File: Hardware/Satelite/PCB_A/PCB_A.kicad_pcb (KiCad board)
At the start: 2 copper layers, 54 x 54 mm, 87 parts, among them J1 Batería LiPo (Soldada), J2 CONUFL001-SMD, J3 Servo Globo, J4 Conector_PCB_A-B, J5 Servo Paracaídas, M1 Spacer, M2 Spacer, M3 Spacer, Q1 SSM3J338R,LF, Q2 BC817, U1 A2235-H, U2 CC1101RGP, U3 0915BM15A0001E, U4 AP9211SA-AF-HAC-7, U5 B39921B3588U410, U6 CC1190, Y1 26 MHz

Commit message: Completado nuevo PCB_A
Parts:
- removed the C1 at (-0.51, -3.42)
- removed the C13 at (-38.6, 24.2)
- removed the C13 at (9.30, 15.1)
- removed the C14 at (13.8, 16.1)
- removed the L1 at (-44.9, 12.7)
- removed the L1 at (10.9, 16.7)
- removed the R10 at (12.1, 15.7)
- removed the R9 at (-44.9, 9.83)
- removed the R9 at (10.9, 14.6)
- removed TP3: TestPoint_P1, TestPoint:TestPoint_Pad_D1.0mm
- added C13: 0.8pF, Capacitor_SMD:C_0402_1005Metric, F.Cu at (7.90, 0.94)
- added G***: LOGO, AXTEC:Logo_AXTEC, F.Cu at (10.9, 17.3)
- added G***: LOGO, AXTEC:Logo_AXTEC, B.Cu at (10.7, 17.3)
- added L1: Bead, Inductor_SMD:L_0402_1005Metric, F.Cu at (13.1, -0.33)
- added R9: 3.3k, Resistor_SMD:R_0402_1005Metric, F.Cu at (2.57, -3.12)
- moved REF** 62.0 mm to (4.34, 11.2)
- moved L3 59.1 mm to (10.4, -2.36), turned to 180 degrees
- moved REF** 58.0 mm to (-8.97, 20.7)
- moved U5 54.2 mm to (7.44, 3.94), turned to 180 degrees
- moved C14 53.8 mm to (7.09, -0.99), turned to 0 degrees
- moved C17 52.8 mm to (4.50, -3.10)
- moved C16 52.7 mm to (10.4, -0.94), turned to 0 degrees
- moved U6 51.8 mm to (1.80, 0.94), turned to 0 degrees
- moved D3 50.9 mm to (0.11, -25.5), turned to 0 degrees
- moved L4 50.6 mm to (6.25, -2.67), turned to 180 degrees
- moved C2 48.7 mm to (-15.6, 16.2)
- moved R3 48.7 mm to (-19.5, 14.2)
- moved C3 48.7 mm to (-15.6, 14.3)
- moved R4 48.7 mm to (-11.7, 13.0)
- moved U1 48.7 mm to (-4.55, 12.1)
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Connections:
- L5 pad 1: +3V3_Internal -> /CC1101/VDD_PA
- U6 pad 6: /CC1101/VDD_PA -> +3V3_Internal
- U6 pad 7: /CC1101/GDO2 -> /CC1101/GDO0
- U6 pad 8: /CC1101/GDO0 -> /CC1101/GDO2
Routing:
- net +3V3_Internal: track 20.5 -> 132.6 mm, vias 1 -> 2
- net /nCHG: track 0.00 -> 47.8 mm
- net +BATT: track 22.7 -> 68.3 mm, vias 4 -> 5
- net /CC1101/GDO0: track 0.00 -> 41.3 mm, vias 0 -> 4
- net GND: track 91.2 -> 124.9 mm, vias 25 -> 36
- net /CC1101/GDO2: track 0.00 -> 30.1 mm, vias 0 -> 4
- net Net-(J4-Pad14): track 0.00 -> 29.0 mm
- net /CS: track 28.5 -> 56.9 mm, vias 2 -> 0
- net Net-(J4-Pad13): track 0.00 -> 22.1 mm
- net /CC1101/VDD_PA: track 0.00 -> 19.1 mm
- net Net-(R6-Pad1): track 0.00 -> 17.6 mm
- net /GPS_TX: track 0.14 -> 15.5 mm, vias 0 -> 2
- net Net-(R7-Pad1): track 0.00 -> 14.5 mm
- net /SDI: track 37.0 -> 26.6 mm
- net Net-(R5-Pad1): track 0.00 -> 10.3 mm
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- added copper zone on F.Cu, net Net-(L2-Pad2)
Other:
- board text added: "PCB_A v2.0"
- board text removed: "BATT"
- board text removed: "PCB_A v1.0"

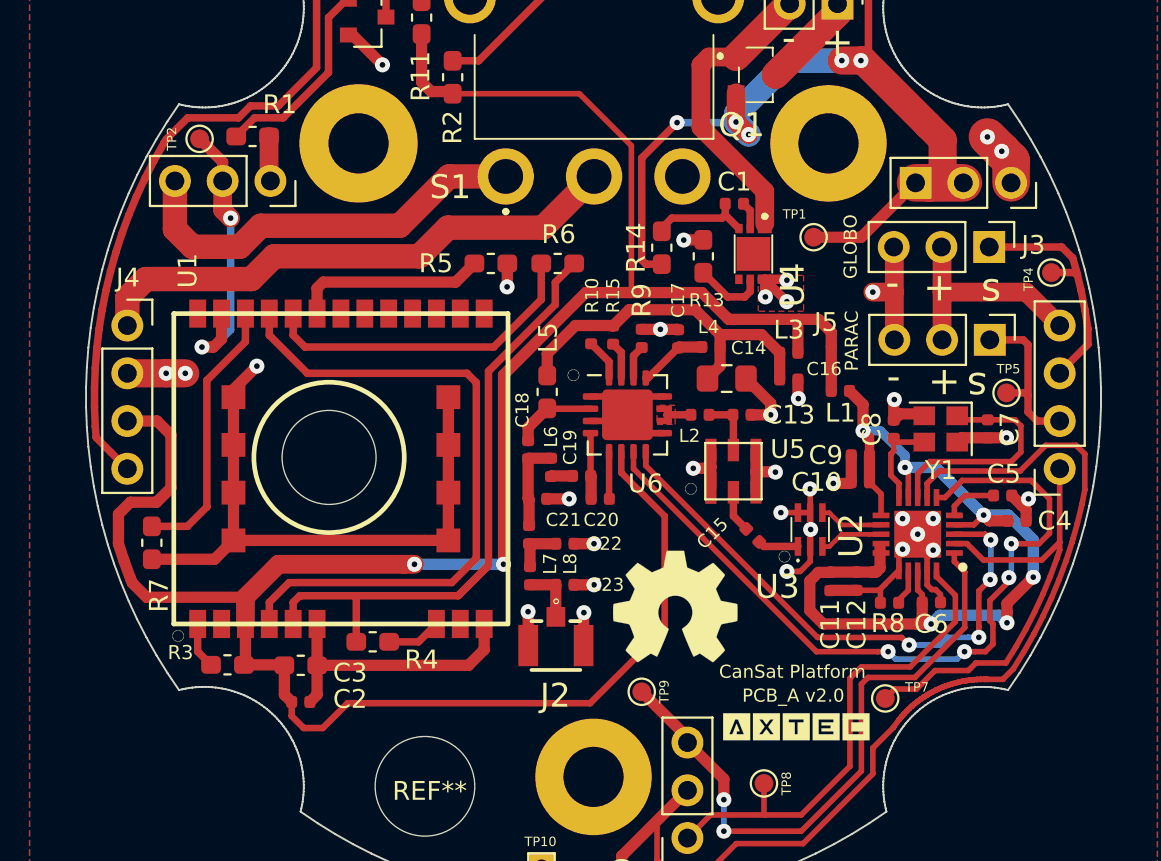
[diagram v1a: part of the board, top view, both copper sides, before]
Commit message: Mejoras al layout RF de PCB_A
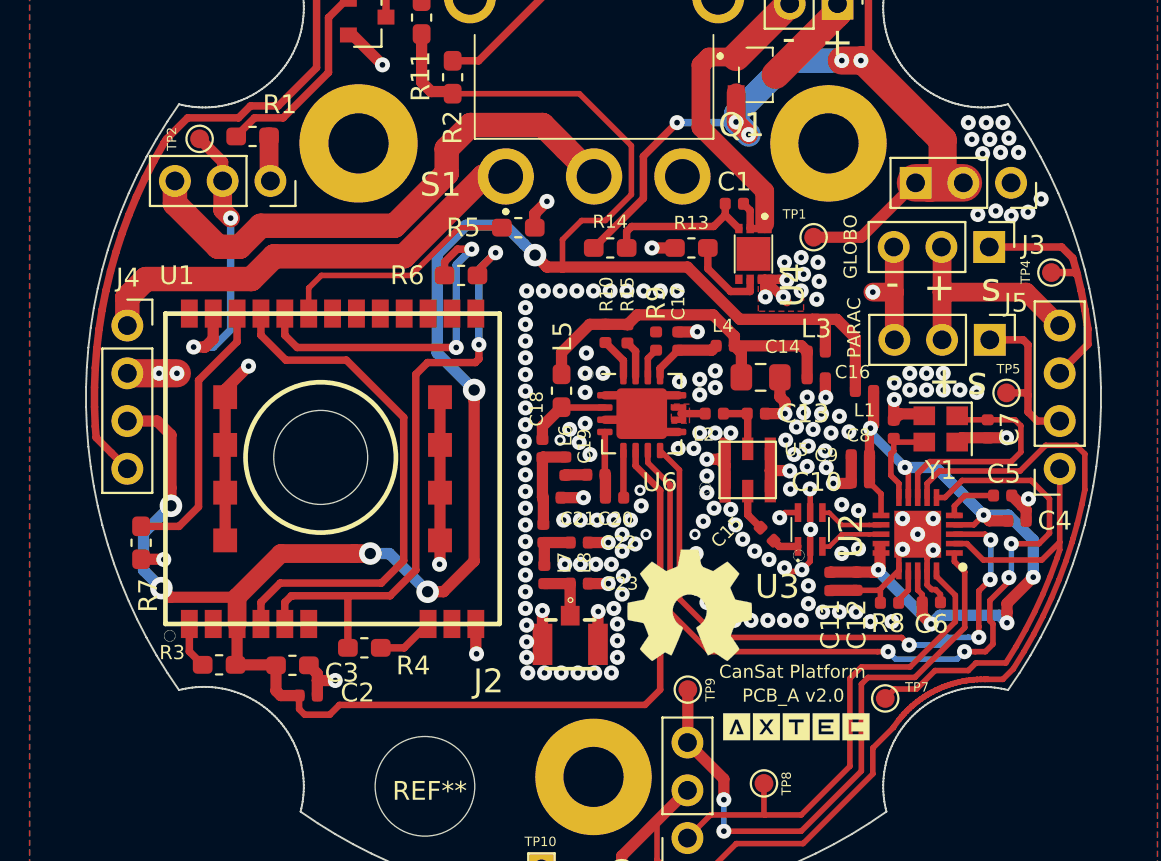
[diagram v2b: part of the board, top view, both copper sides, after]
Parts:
- moved R6 5.18 mm to (-7.05, -6.48)
- moved R14 2.74 mm to (0.89, -7.94), turned to 180 degrees
- moved TP9 2.45 mm to (5.02, 15.6)
- moved R5 2.40 mm to (-4.00, -9.02)
- moved C14 1.80 mm to (8.89, -1.05)
- moved C16 1.46 mm to (11.8, -1.00)
- moved L3 1.46 mm to (11.8, -2.43)
- moved L1 1.28 mm to (14.4, -0.33)
- moved R13 0.78 mm to (5.21, -7.94), turned to 0 degrees
- moved R9 0.77 mm to (3.33, -2.98)
- moved REF** 0.76 mm to (5.11, 11.1)
- moved C13 0.76 mm to (8.66, 0.88)
- moved C15 0.76 mm to (9.23, 7.29)
- moved U5 0.76 mm to (8.20, 3.87)
- moved C23 0.76 mm to (-0.76, 9.92)
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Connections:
- S1 pad 1: Net-(J4-Pad13) -> Net-(J4-Pad14)
- S1 pad 2: Net-(J4-Pad14) -> Net-(J4-Pad13)
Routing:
- net GND: track 124.9 -> 96.2 mm, vias 36 -> 193
- net +3V3_Internal: track 132.6 -> 144.5 mm, vias 2 -> 6
- net Net-(U1-Pad19): track 35.7 -> 27.8 mm
- net Net-(J4-Pad13): track 22.1 -> 29.0 mm
- net VDD: track 49.9 -> 43.5 mm, vias 6 -> 7
- net Net-(J4-Pad14): track 29.0 -> 24.3 mm
- net /CC1101/GDO0: track 41.3 -> 44.4 mm
- net /CC1101/GDO2: track 30.1 -> 32.9 mm
- net Net-(C1-Pad1): track 5.28 -> 8.10 mm
- net Net-(R5-Pad1): track 10.3 -> 13.0 mm
- net /GPS/GPS_1V8: track 34.8 -> 33.0 mm, vias 0 -> 2
- net Net-(R6-Pad1): track 17.6 -> 18.6 mm, vias 0 -> 2
- net Net-(C1-Pad2): track 17.4 -> 18.2 mm
- net +BATT: track 68.3 -> 67.5 mm
- net Net-(C15-Pad2): track 2.16 -> 1.43 mm
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
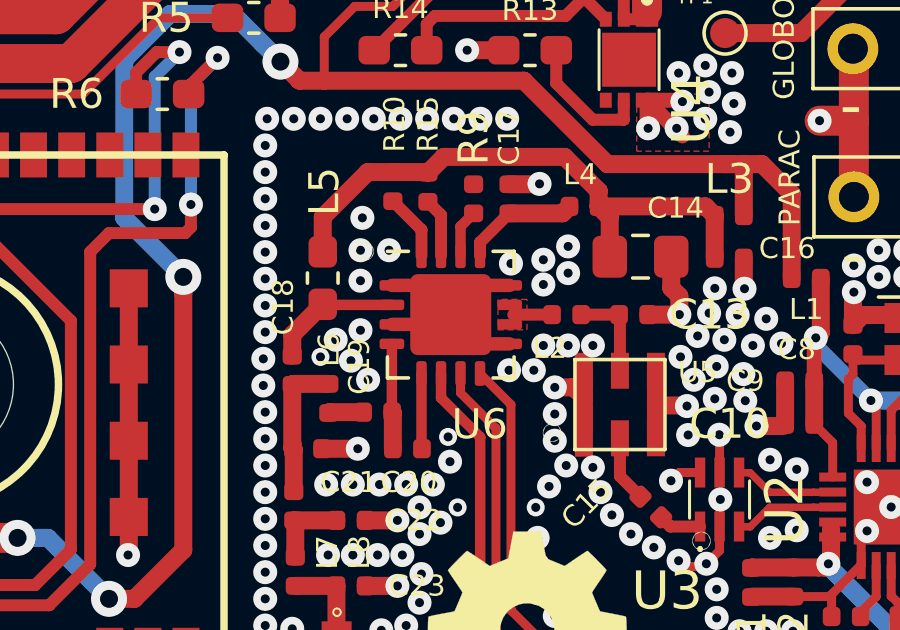
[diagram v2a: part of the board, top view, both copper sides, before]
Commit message: Nuevo PCB de estación terrena con CC1190
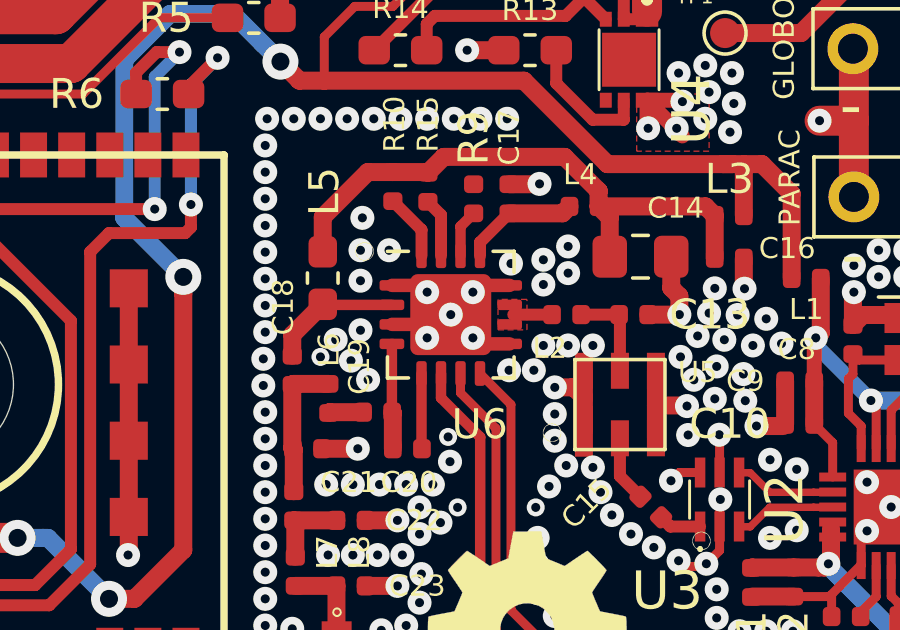
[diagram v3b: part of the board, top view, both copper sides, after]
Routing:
- net GND: vias 193 -> 198
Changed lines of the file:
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@@
     (thickness 1.6)
     (drawings 39)
-    (tracks 942)
+    (tracks 947)
     (zones 0)
     (modules 82)
@@
     (effects (font (size 0.7 0.7) (thickness 0.175)))
   )
+  (via (at 2.5654 0.8763) (size 0.8) (drill 0.3) (layers F.Cu B.Cu) (net 1))
+  (via (at 3.302 0.127) (size 0.8) (drill 0.3) (layers F.Cu B.Cu) (net 1))
+  (via (at 3.302 1.651) (size 0.8) (drill 0.3) (layers F.Cu B.Cu) (net 1))
+  (via (at 1.778 1.651) (size 0.8) (drill 0.3) (layers F.Cu B.Cu) (net 1))
+  (via (at 1.778 0.127) (size 0.8) (drill 0.3) (layers F.Cu B.Cu) (net 1))
   (via (at -1.778 2.286) (size 0.6) (drill 0.3) (layers F.Cu B.Cu) (net 1))
   (via (at 7.3025 1.905) (size 0.8) (drill 0.3) (layers F.Cu B.Cu) (net 1))
@@
     (connect_pads (clearance 0.25))
     (min_thickness 0.25)
-    (fill yes (arc_segments 32) (thermal_gap 0.3) (thermal_bridge_width 0.8))
+    (fill yes (arc_segments 32) (thermal_gap 0.25) (thermal_bridge_width 0.8))
     (polygon
       (pts
@@
     (connect_pads (clearance 0.25))
     (min_thickness 0.25)
-    (fill yes (arc_segments 32) (thermal_gap 0.3) (thermal_bridge_width 0.8))
+    (fill yes (arc_segments 32) (thermal_gap 0.25) (thermal_bridge_width 0.8))
     (polygon
       (pts

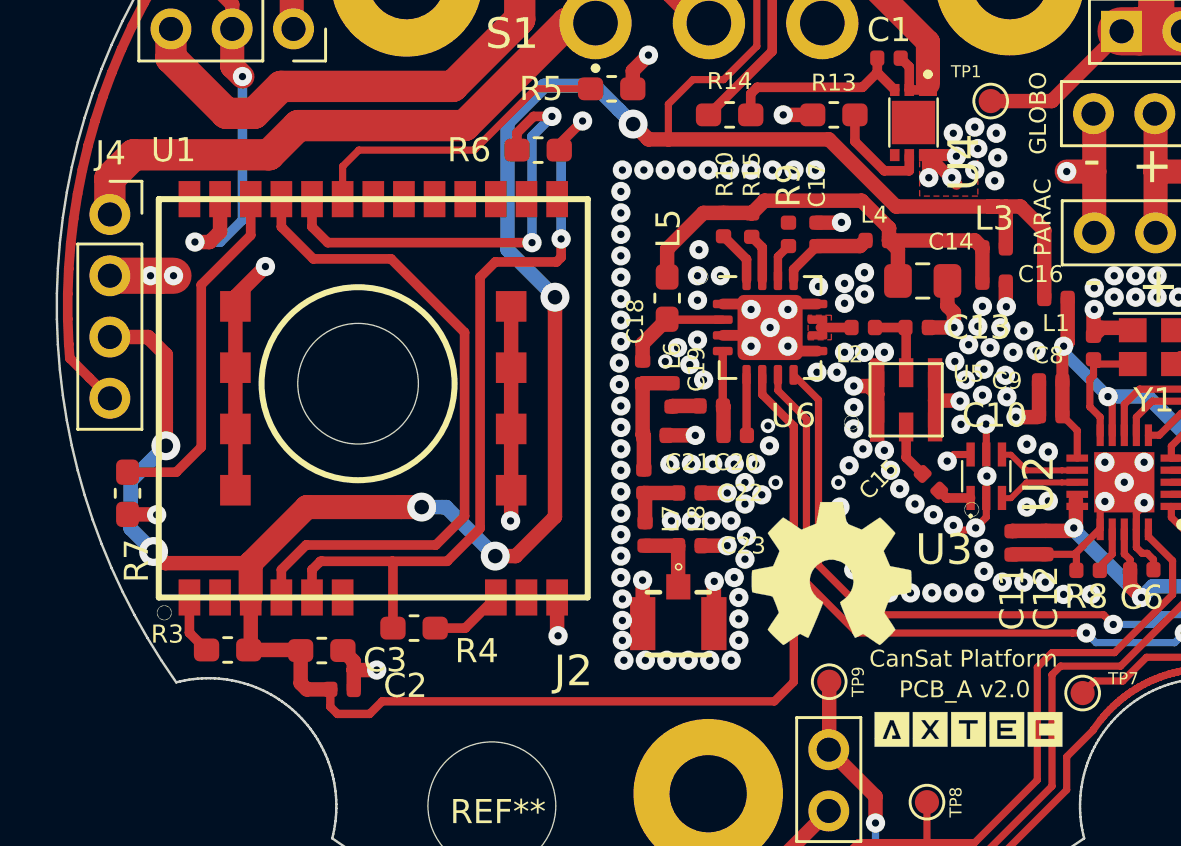
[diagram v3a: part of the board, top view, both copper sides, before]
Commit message: Corrección de silkscreen PCB_C
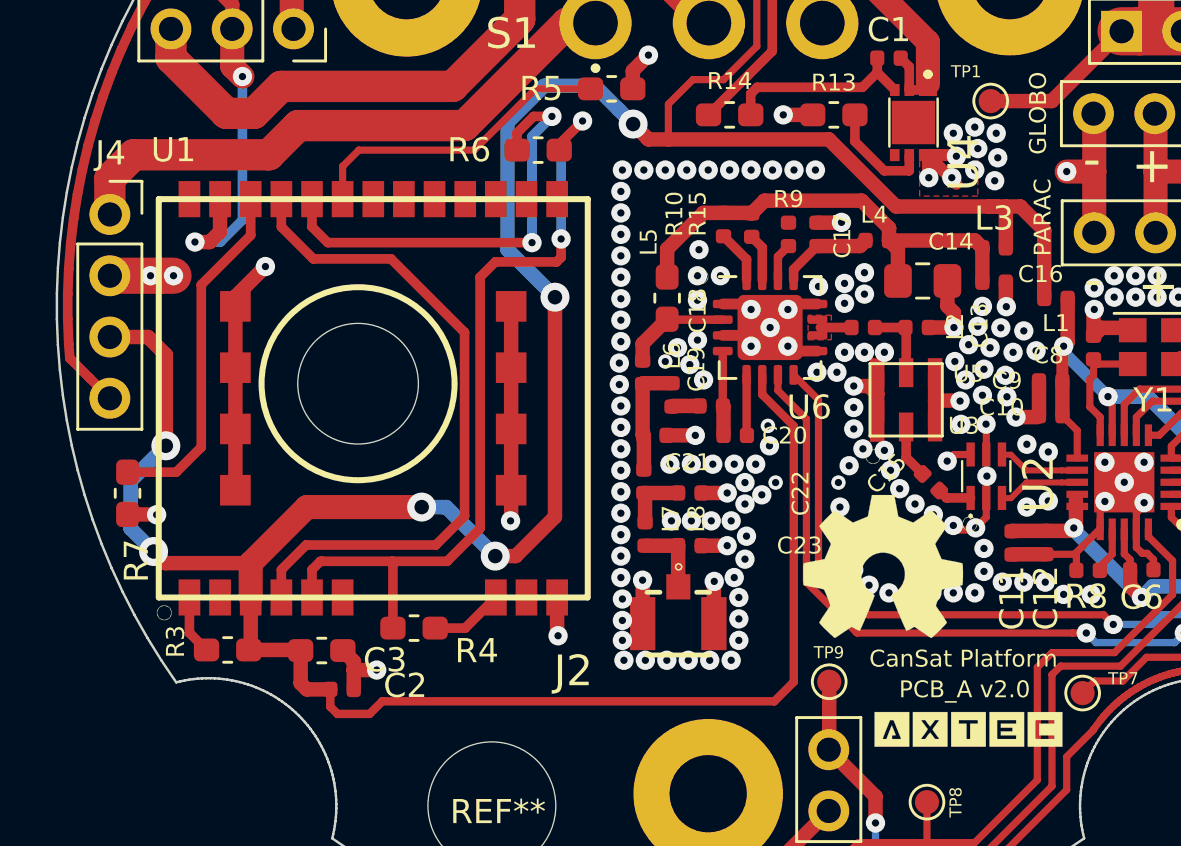
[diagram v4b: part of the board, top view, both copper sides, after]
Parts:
- moved REF** 2.15 mm to (7.24, 10.8)
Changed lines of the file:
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@@
     (tags "QFN NoLead")
     (attr smd)
-    (fp_text reference U6 (at 0.9652 3.6576) (layer F.SilkS)
+    (fp_text reference U6 (at 1.6256 3.3147) (layer F.SilkS)
       (effects (font (size 1 1) (thickness 0.15)))
     )
@@
     (tags resistor)
     (attr smd)
-    (fp_text reference R15 (at 2.1058 0 90) (layer F.SilkS)
+    (fp_text reference R15 (at 0.4675 -2.2352 90) (layer F.SilkS)
       (effects (font (size 0.7 0.7) (thickness 0.15)))
     )
@@
     (tags resistor)
     (attr smd)
-    (fp_text reference R10 (at 2.0828 0.0508 90) (layer F.SilkS)
+    (fp_text reference R10 (at 0.4445 -2.032 90) (layer F.SilkS)
       (effects (font (size 0.7 0.7) (thickness 0.15)))
     )
@@
     (tags resistor)
     (attr smd)
-    (fp_text reference R9 (at 2.032 0 90) (layer F.SilkS)
-      (effects (font (size 1 1) (thickness 0.15)))
+    (fp_text reference R9 (at 1.4605 0 180) (layer F.SilkS)
+      (effects (font (size 0.7 0.7) (thickness 0.15)))
     )
     (fp_text value 3.3k (at 0 1.17 90) (layer F.Fab)
@@
     (tags "inductor handsolder")
     (attr smd)
-    (fp_text reference L5 (at -2.8842 -0.0508 270) (layer F.SilkS)
-      (effects (font (size 1 1) (thickness 0.15)))
+    (fp_text reference L5 (at -2.3241 0.762 270) (layer F.SilkS)
+      (effects (font (size 0.7 0.7) (thickness 0.15)))
     )
     (fp_text value 22nH (at 0 1.43 270) (layer F.Fab)
@@
     (tags inductor)
     (attr smd)
-    (fp_text reference L2 (at 0.5588 -1.1176 180) (layer F.SilkS)
+    (fp_text reference L2 (at -3.81 0.0381 270) (layer F.SilkS)
       (effects (font (size 0.7 0.7) (thickness 0.15)))
     )
@@
     (tags capacitor)
     (attr smd)
-    (fp_text reference C23 (at 2.2074 0) (layer F.SilkS)
+    (fp_text reference C23 (at 4.5442 0) (layer F.SilkS)
       (effects (font (size 0.7 0.7) (thickness 0.15)))
     )
@@
     (tags capacitor)
     (attr smd)
-    (fp_text reference C22 (at 2.1058 0) (layer F.SilkS)
+    (fp_text reference C22 (at 4.595 0.0127 90) (layer F.SilkS)
       (effects (font (size 0.7 0.7) (thickness 0.15)))
     )
@@
     (tags capacitor)
     (attr smd)
-    (fp_text reference C20 (at 0.0508 1.1176) (layer F.SilkS)
+    (fp_text reference C20 (at 2.055 0.0127) (layer F.SilkS)
       (effects (font (size 0.7 0.7) (thickness 0.15)))
     )
@@
     (tags capacitor)
     (attr smd)
-    (fp_text reference C18 (at -2.1106 0.3048 270) (layer F.SilkS)
+    (fp_text reference C18 (at -2.5551 -2.286 270) (layer F.SilkS)
       (effects (font (size 0.7 0.7) (thickness 0.15)))
     )
@@
     (tags capacitor)
     (attr smd)
-    (fp_text reference C17 (at 2.055 0 90) (layer F.SilkS)
+    (fp_text reference C17 (at -0.0635 1.0541 90) (layer F.SilkS)
       (effects (font (size 0.7 0.7) (thickness 0.15)))
     )
@@
     (tags capacitor)
     (attr smd)
-    (fp_text reference C13 (at 2.54 0) (layer F.SilkS)
-      (effects (font (size 1 1) (thickness 0.15)))
+    (fp_text reference C13 (at 2.5908 -0.0889 90) (layer F.SilkS)
+      (effects (font (size 0.7 0.7) (thickness 0.15)))
     )
     (fp_text value 0.8pF (at 0 1.17) (layer F.Fab)
@@
     (tags capacitor)
     (attr smd)
-    (fp_text reference C15 (at -1.598419 1.436841 45) (layer F.SilkS)
+    (fp_text reference C15 (at -1.553518 1.05069 45) (layer F.SilkS)
       (effects (font (size 0.7 0.7) (thickness 0.15)))
     )
@@
     (tags "resistor handsolder")
     (attr smd)
-    (fp_text reference R3 (at 2.499 0.651 180) (layer F.SilkS)
+    (fp_text reference R3 (at 2.1561 0.3462 270) (layer F.SilkS)
       (effects (font (size 0.75 0.75) (thickness 0.15)))
     )
@@
     (tags capacitor)
     (attr smd)
-    (fp_text reference C10 (at 2.33 0.01 180) (layer F.SilkS)
-      (effects (font (size 1 1) (thickness 0.15)))
+    (fp_text reference C10 (at 2.0294 0.339 180) (layer F.SilkS)
+      (effects (font (size 0.7 0.7) (thickness 0.15)))
     )
     (fp_text value 100nF (at 0 1.17 180) (layer F.Fab)
@@
     (tags Filter)
     (attr smd)
-    (fp_text reference U3 (at 1.747 -3.0438) (layer F.SilkS)
-      (effects (font (size 1.27 1.27) (thickness 0.254)))
+    (fp_text reference U3 (at 0.9342 2.087) (layer F.SilkS)
+      (effects (font (size 0.7 0.7) (thickness 0.15)))
     )
     (fp_text value 0915BM15A0001E (at 0 -0.15 180) (layer F.SilkS) hide
@@
   )
   (module Symbol:OSHW-Symbol_6.7x6mm_SilkScreen locked (layer F.Cu)
-    (at 5.1054 11.0871)
+    (at 7.239 10.795)
     (descr "Open Source Hardware Symbol")
     (tags "Logo Symbol OSHW")
@@
     (tags "test point SMD pad")
     (attr virtual)
-    (fp_text reference TP9 (at 1.2 0 90) (layer F.SilkS)
+    (fp_text reference TP9 (at -0.0127 -1.2065) (layer F.SilkS)
       (effects (font (size 0.5 0.5) (thickness 0.125)))
     )
@@
   (gr_poly (pts (xy -3.175 16.0655) (xy -4.3815 16.0655) (xy -4.41325 -6.223) (xy -3.2385 -6.223)) (layer F.Mask) (width 0.1))
   (gr_circle (center -0.3048 -1.2319) (end -0.2948 -1.2319) (layer F.SilkS) (width 0.6))
-  (gr_circle (center 10.922 8.4201) (end 10.932 8.4201) (layer F.SilkS) (width 0.6))
-  (gr_circle (center 5.9436 4.8133) (end 5.9436 4.8233) (layer F.SilkS) (width 0.6))
+  (gr_circle (center 10.8458 9.017) (end 10.8558 9.017) (layer F.SilkS) (width 0.6))
+  (gr_circle (center 6.8326 6.223) (end 6.8326 6.233) (layer F.SilkS) (width 0.6))
   (gr_circle (center -22.5425 12.7) (end -22.5325 12.7) (layer F.SilkS) (width 0.6))
   (gr_text s (at 20.4048 -0.5882 180) (layer B.SilkS)
